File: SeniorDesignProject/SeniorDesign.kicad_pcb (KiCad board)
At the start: 2 copper layers, 69.8 x 63.5 mm, 35 parts, among them J1 RJ45(LoadCells), J2 RJ45(Accelerometer), J3 PICkit3, J5 ID-12LA Header, J6 XBEE Header, J7 7-Segment Display, P7 Power 1, U1 INA827, U2 LM1117-3.3, U3 ICL7660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

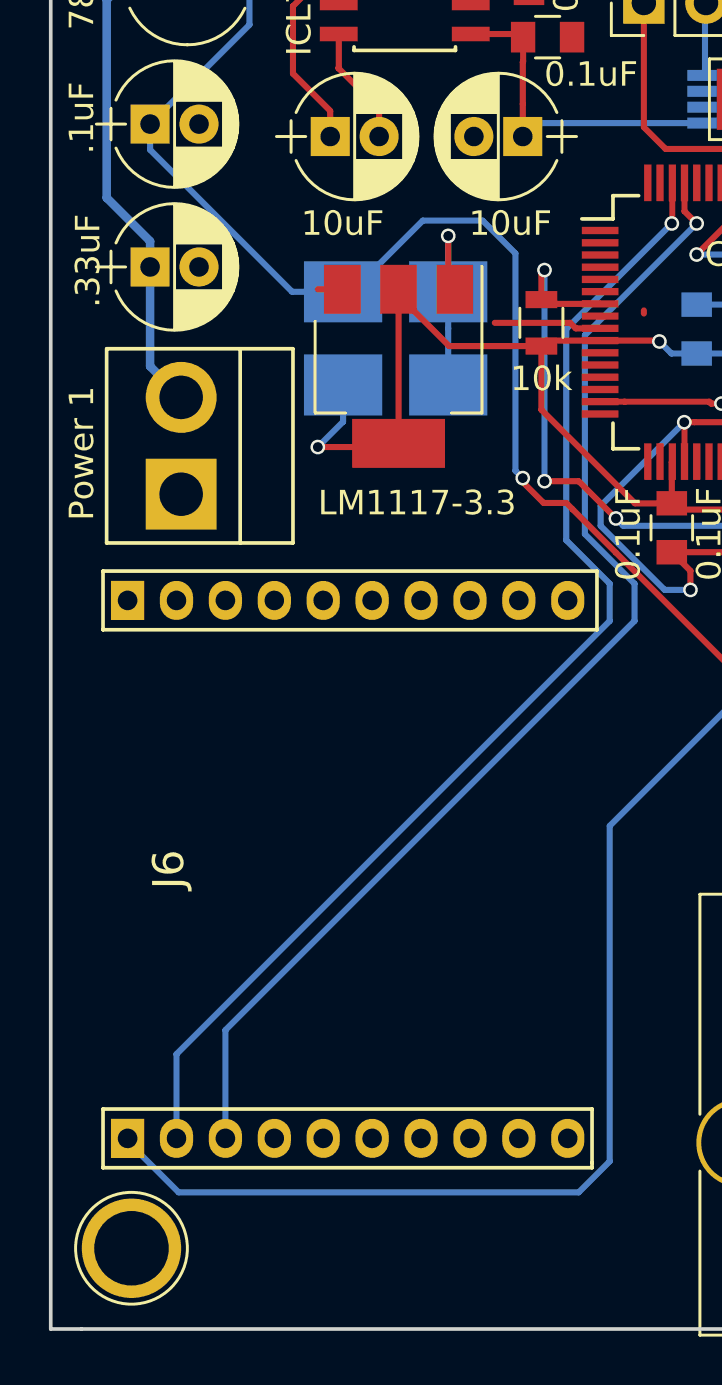
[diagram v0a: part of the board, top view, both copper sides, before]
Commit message: Version 2 updates 3.3V regulator with GND, 5V regulator with GND, and added via
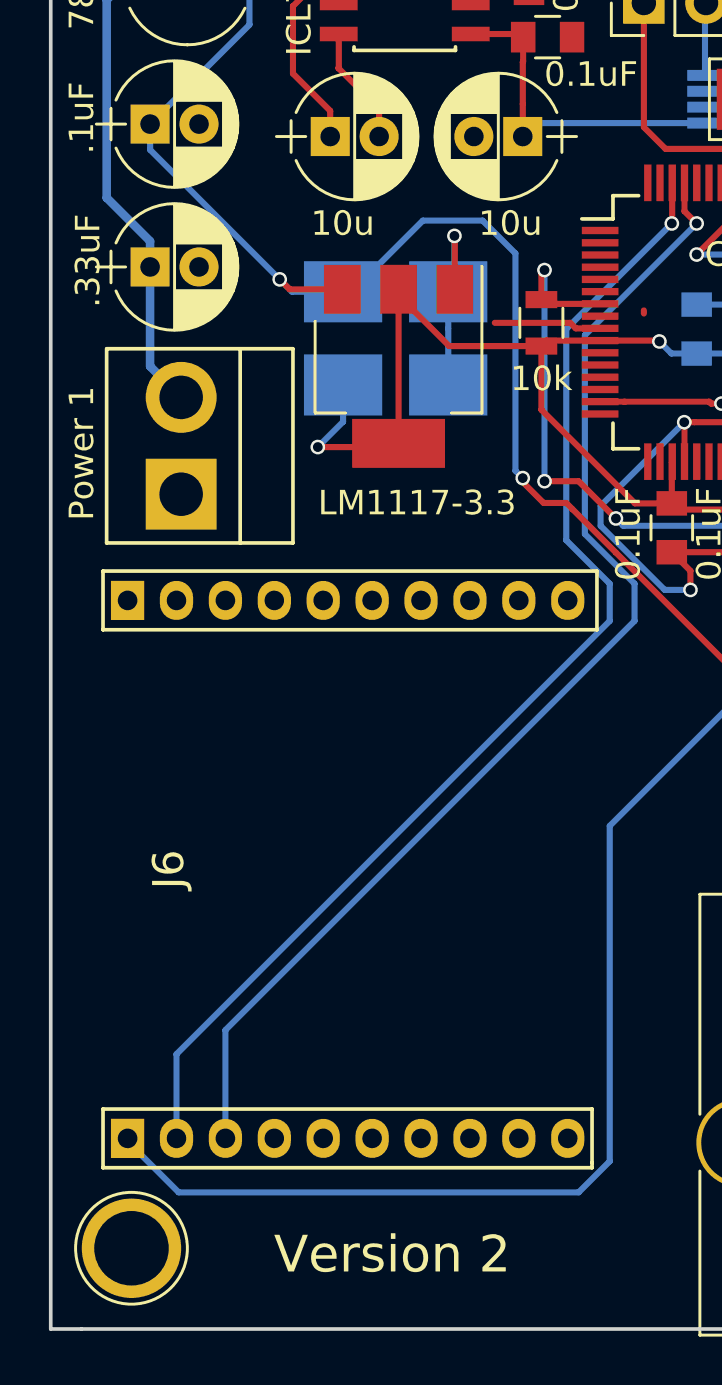
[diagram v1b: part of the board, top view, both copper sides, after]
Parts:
- C10, C9: value 10uF -> 10u
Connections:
- C13 pad 2: Net-(C13-Pad2) -> GND
- C14 pad 2: Net-(C13-Pad2) -> GND
- U2 pad 1: Net-(C13-Pad2) -> GND
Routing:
- net Net-(C13-Pad2): track 8.39 -> 3.81 mm, vias 1 -> 0
- net GND: track 35.6 -> 40.0 mm, vias 4 -> 5
- net +5V: track 143.0 -> 144.1 mm, vias 1 -> 2
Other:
- board text added: "Version 2"
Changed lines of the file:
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@@
 (kicad_pcb (version 4) (host pcbnew 4.0.6-e0-6349~53~ubuntu16.04.1)
   (general
-    (links 83)
-    (no_connects 1)
-    (area 115.494999 56.175 185.495001 121.423)
+    (links 80)
+    (no_connects 2)
+    (area 115.494999 57.074999 185.495001 120.725001)
     (thickness 1.6)
-    (drawings 7)
-    (tracks 399)
+    (drawings 8)
+    (tracks 403)
     (zones 0)
     (modules 35)
@@
     (32 B.Adhes user)
     (33 F.Adhes user)
-    (34 B.Paste user hide)
+    (34 B.Paste user)
     (35 F.Paste user)
     (36 B.SilkS user)
     (37 F.SilkS user)
-    (38 B.Mask user hide)
-    (39 F.Mask user hide)
-    (40 Dwgs.User user hide)
-    (41 Cmts.User user hide)
-    (42 Eco1.User user hide)
-    (43 Eco2.User user hide)
+    (38 B.Mask user)
+    (39 F.Mask user)
+    (40 Dwgs.User user)
+    (41 Cmts.User user)
+    (42 Eco1.User user)
+    (43 Eco2.User user)
     (44 Edge.Cuts user)
-    (45 Margin user hide)
-    (46 B.CrtYd user hide)
-    (47 F.CrtYd user hide)
+    (45 Margin user)
+    (46 B.CrtYd user)
+    (47 F.CrtYd user)
     (48 B.Fab user)
     (49 F.Fab user)
@@
     (mod_text_size 1 1)
     (mod_text_width 0.15)
-    (pad_size 1.52 1.52)
-    (pad_drill 0.8)
+    (pad_size 3.2 2.5)
+    (pad_drill 0)
     (pad_to_mask_clearance 0.2)
     (aux_axis_origin 0 0)
-    (visible_elements FFFFF7E1)
+    (visible_elements FFFFFFFF)
     (pcbplotparams
       (layerselection 0x00030_80000001)
@@
       (effects (font (size 1 1) (thickness 0.15)))
     )
-    (fp_text value 10uF (at 0.508 3.556) (layer F.SilkS)
+    (fp_text value 10u (at 0.508 3.556) (layer F.SilkS)
       (effects (font (size 1 1) (thickness 0.15)))
     )
@@
       (net 42 +5V))
     (pad 1 smd rect (at -3.15 -2.3 270) (size 2 1.5) (layers F.Cu F.Paste F.Mask)
-      (net 94 "Net-(C13-Pad2)"))
+      (net 36 GND))
     (model TO_SOT_Packages_SMD.3dshapes/SOT-223.wrl
       (at (xyz 0 0 0))
@@
       (effects (font (size 1 1) (thickness 0.15)))
     )
-    (fp_text value 10uF (at 0.508 -3.556 180) (layer F.SilkS)
+    (fp_text value 10u (at 0.508 -3.556 180) (layer F.SilkS)
       (effects (font (size 1 1) (thickness 0.15)))
     )
@@
       (net 42 +5V))
     (pad 2 smd rect (at 2.15 0) (size 3.2 2.5) (layers B.Cu B.Paste B.Mask)
-      (net 94 "Net-(C13-Pad2)"))
+      (net 36 GND))
     (model Capacitors_Tantalum_SMD.3dshapes/CP_Tantalum_Case-T_EIA-3528-12.wrl
       (at (xyz 0 0 0))
@@
       (net 38 3.3V))
     (pad 2 smd rect (at 2.15 0) (size 3.2 2.5) (layers B.Cu B.Paste B.Mask)
-      (net 94 "Net-(C13-Pad2)"))
+      (net 36 GND))
     (model Capacitors_Tantalum_SMD.3dshapes/CP_Tantalum_Case-T_EIA-3528-12.wrl
       (at (xyz 0 0 0))
@@
       (rotate (xyz 0 0 0))
     )
+  )
+  (gr_text "Version 2" (at 129.54 117.602) (layer F.SilkS)
+    (effects (font (size 1.5 1.5) (thickness 0.3)))
   )
   (gr_line (start 115.57 120.65) (end 116.84 120.65) (angle 90) (layer Edge.Cuts) (width 0.15))
@@
   )
   (segment (start 139.827 78.994) (end 139.827 79.121) (width 0.25) (layer F.Cu) (net 0))
+  (segment (start 132.08 75.946) (end 132.08 77.34159) (width 0.25) (layer B.Cu) (net 36))
+  (segment (start 132.08 77.34159) (end 131.6396 77.78199) (width 0.25) (layer B.Cu) (net 36))
+  (segment (start 131.6396 77.78199) (end 131.507795 77.913795) (width 0.25) (layer B.Cu) (net 36))
+  (segment (start 132.094 78.13) (end 132.094 75.96) (width 0.25) (layer F.Cu) (net 36))
+  (via (at 132.08 75.946) (size 0.6) (drill 0.4) (layers F.Cu B.Cu) (net 36))
+  (segment (start 132.094 75.96) (end 132.08 75.946) (width 0.25) (layer F.Cu) (net 36))
   (segment (start 141.732 90.424) (end 141.732 89.646) (width 0.25) (layer F.Cu) (net 36))
   (segment (start 141.732 89.646) (end 140.97 88.884) (width 0.25) (layer F.Cu) (net 36))
@@
   (segment (start 149.351 70.683) (end 147.701 70.683) (width 0.25) (layer B.Cu) (net 41))
   (segment (start 147.701 70.683) (end 146.726 70.683) (width 0.25) (layer B.Cu) (net 41))
+  (segment (start 125.442 78.232) (end 124.934 77.724) (width 0.25) (layer B.Cu) (net 42))
+  (segment (start 124.934 77.724) (end 119.634 72.424) (width 0.25) (layer B.Cu) (net 42))
+  (segment (start 127.494 78.13) (end 125.34 78.13) (width 0.25) (layer F.Cu) (net 42))
+  (segment (start 125.34 78.13) (end 124.934 77.724) (width 0.25) (layer F.Cu) (net 42))
+  (via (at 124.934 77.724) (size 0.6) (drill 0.4) (layers F.Cu B.Cu) (net 42))
   (segment (start 123.698 65.532) (end 123.698 67.31) (width 0.25) (layer B.Cu) (net 42))
   (segment (start 123.698 67.31) (end 119.634 71.374) (width 0.25) (layer B.Cu) (net 42))
   (segment (start 127.526 78.232) (end 125.442 78.232) (width 0.25) (layer B.Cu) (net 42))
-  (segment (start 125.442 78.232) (end 119.634 72.424) (width 0.25) (layer B.Cu) (net 42))
   (segment (start 119.634 72.424) (end 119.634 71.374) (width 0.25) (layer B.Cu) (net 42))
-  (segment (start 126.494 78.13) (end 127.494 78.13) (width 0.25) (layer F.Cu) (net 42))
   (segment (start 134.874 85.852) (end 134.574001 85.552001) (width 0.25) (layer B.Cu) (net 42))
   (segment (start 134.574001 85.552001) (end 134.574001 76.662001) (width 0.25) (layer B.Cu) (net 42))
@@
   (segment (start 130.787001 75.320999) (end 127.876 78.232) (width 0.25) (layer B.Cu) (net 42))
   (segment (start 127.876 78.232) (end 127.526 78.232) (width 0.25) (layer B.Cu) (net 42))
-  (segment (start 127.032 77.668) (end 127.494 78.13) (width 0.25) (layer F.Cu) (net 42))
   (segment (start 136.652 86.868) (end 135.726998 86.868) (width 0.25) (layer F.Cu) (net 42))
   (segment (start 135.726998 86.868) (end 134.874 86.015002) (width 0.25) (layer F.Cu) (net 42))
@@
   (segment (start 131.826 78.232) (end 131.826 79.732) (width 0.25) (layer B.Cu) (net 94))
   (segment (start 131.826 79.732) (end 131.826 82.042) (width 0.25) (layer B.Cu) (net 94))
-  (segment (start 131.826 75.946) (end 131.826 77.862) (width 0.25) (layer F.Cu) (net 94))
-  (segment (start 131.826 77.862) (end 132.094 78.13) (width 0.25) (layer F.Cu) (net 94))
-  (segment (start 131.826 78.232) (end 131.826 75.946) (width 0.25) (layer B.Cu) (net 94))
-  (via (at 131.826 75.946) (size 0.6) (drill 0.4) (layers F.Cu B.Cu) (net 94))
   (zone (net 36) (net_name GND) (layer F.Cu) (hatch edge 0.508)
     (connect_pads (clearance 0.508))

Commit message: Updates to board
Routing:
- net Net-(C13-Pad2): track 3.81 -> 0.00 mm
- net GND: track 40.0 -> 43.8 mm
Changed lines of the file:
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@@
 (kicad_pcb (version 4) (host pcbnew 4.0.6-e0-6349~53~ubuntu16.04.1)
   (general
-    (links 80)
-    (no_connects 2)
-    (area 115.494999 57.074999 185.495001 120.725001)
+    (links 84)
+    (no_connects 0)
+    (area 115.494999 56.175 185.495001 121.423)
     (thickness 1.6)
     (drawings 8)
@@
     (zones 0)
     (modules 35)
-    (nets 95)
+    (nets 94)
   )
   (page USLetter)
@@
   (net 92 "Net-(C9-Pad1)")
   (net 93 "Net-(C9-Pad2)")
-  (net 94 "Net-(C13-Pad2)")
   (net_class Default "This is the default net class."
     (clearance 0.2)
@@
     (add_net MISO)
     (add_net MOSI)
-    (add_net "Net-(C13-Pad2)")
     (add_net "Net-(C8-Pad1)")
     (add_net "Net-(C9-Pad1)")
@@
       (effects (font (size 1 1) (thickness 0.15)))
     )
-    (fp_text value 1pin (at 0 3) (layer F.Fab)
+    (fp_text value 1pin (at 0 3) (layer F.Fab) hide
       (effects (font (size 1 1) (thickness 0.15)))
     )
@@
       (effects (font (size 1 1) (thickness 0.15)))
     )
-    (fp_text value 1pin (at 0 3) (layer F.Fab)
+    (fp_text value 1pin (at 0 3) (layer F.Fab) hide
       (effects (font (size 1 1) (thickness 0.15)))
     )
@@
     (descr "module 1 pin (ou trou mecanique de percage)")
     (tags DEV)
-    (fp_text reference REF** (at 0 -3.048) (layer F.Fab)
-      (effects (font (size 1 1) (thickness 0.15)))
-    )
-    (fp_text value 1pin (at 0 3) (layer F.Fab)
+    (fp_text reference REF** (at 0 -3.048) (layer F.Fab) hide
+      (effects (font (size 1 1) (thickness 0.15)))
+    )
+    (fp_text value 1pin (at 0 3) (layer F.Fab) hide
       (effects (font (size 1 1) (thickness 0.15)))
     )
@@
     (descr "module 1 pin (ou trou mecanique de percage)")
     (tags DEV)
-    (fp_text reference REF** (at 0 -3.048) (layer F.Fab)
-      (effects (font (size 1 1) (thickness 0.15)))
-    )
-    (fp_text value 1pin (at 0 3) (layer F.Fab)
+    (fp_text reference REF** (at 0 -3.048) (layer F.Fab) hide
+      (effects (font (size 1 1) (thickness 0.15)))
+    )
+    (fp_text value 1pin (at 0 3) (layer F.Fab) hide
       (effects (font (size 1 1) (thickness 0.15)))
     )
@@
   (segment (start 144.018 78.756) (end 146.05 78.756) (width 0.25) (layer B.Cu) (net 36) (status 30))
   (segment (start 144.018 78.756) (end 141.986 78.756) (width 0.25) (layer B.Cu) (net 36) (status 30))
+  (segment (start 131.826 78.232) (end 131.826 79.732) (width 0.25) (layer B.Cu) (net 36))
+  (segment (start 131.826 79.732) (end 131.826 82.042) (width 0.25) (layer B.Cu) (net 36))
   (segment (start 142.326 71.333) (end 135.423 71.333) (width 0.25) (layer B.Cu) (net 37))
   (segment (start 135.423 71.333) (end 134.874 71.882) (width 0.25) (layer B.Cu) (net 37))
@@
   (segment (start 129 70.75063) (end 127.33737 69.088) (width 0.25) (layer F.Cu) (net 93))
   (segment (start 127.823 67.691) (end 127.348 67.691) (width 0.25) (layer F.Cu) (net 93))
-  (segment (start 131.826 78.232) (end 131.826 79.732) (width 0.25) (layer B.Cu) (net 94))
-  (segment (start 131.826 79.732) (end 131.826 82.042) (width 0.25) (layer B.Cu) (net 94))
   (zone (net 36) (net_name GND) (layer F.Cu) (hatch edge 0.508)
     (connect_pads (clearance 0.508))

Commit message: updates
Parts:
- ? (x2): value 1pin -> (none)
- ? (x2): renamed from REF**; value 1pin -> (none)
- renumbered G*** to ?
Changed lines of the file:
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@@
     (links 84)
     (no_connects 0)
-    (area 115.494999 56.175 185.495001 121.423)
+    (area 115.494999 57.074999 185.495001 120.725001)
     (thickness 1.6)
     (drawings 8)
@@
     (mod_text_size 1 1)
     (mod_text_width 0.15)
-    (pad_size 3.2 2.5)
-    (pad_drill 0)
+    (pad_size 4.064 4.064)
+    (pad_drill 3.048)
     (pad_to_mask_clearance 0.2)
     (aux_axis_origin 0 0)
@@
   (module SeniorDesignFootprints:AkronZ (layer F.Cu)
     (at 170.307 71.374)
-    (fp_text reference G*** (at -0.08 -9.45) (layer F.SilkS) hide
+    (fp_text reference "" (at -0.08 -9.45) (layer F.SilkS) hide
       (effects (font (thickness 0.3)))
     )
@@
       (effects (font (size 1 1) (thickness 0.15)))
     )
-    (fp_text value 1pin (at 0 3) (layer F.Fab) hide
+    (fp_text value "" (at 0 3) (layer F.Fab) hide
       (effects (font (size 1 1) (thickness 0.15)))
     )
@@
     (fp_circle (center 0 0) (end 2.6 0) (layer F.CrtYd) (width 0.05))
     (fp_circle (center 0 0) (end 0 -2.286) (layer F.SilkS) (width 0.12))
-    (pad 1 thru_hole circle (at 0 0) (size 4.064 4.064) (drill 3.048) (layers *.Cu *.Mask))
+    (pad "" np_thru_hole circle (at 0 0) (size 4.064 4.064) (drill 3.048) (layers *.Cu *.Mask))
   )
   (module Connectors:1pin (layer F.Cu)
@@
       (effects (font (size 1 1) (thickness 0.15)))
     )
-    (fp_text value 1pin (at 0 3) (layer F.Fab) hide
+    (fp_text value "" (at 0 3) (layer F.Fab) hide
       (effects (font (size 1 1) (thickness 0.15)))
     )
@@
     (fp_circle (center 0 0) (end 2.6 0) (layer F.CrtYd) (width 0.05))
     (fp_circle (center 0 0) (end 0 -2.286) (layer F.SilkS) (width 0.12))
-    (pad 1 thru_hole circle (at 0 0) (size 4.064 4.064) (drill 3.048) (layers *.Cu *.Mask))
+    (pad "" np_thru_hole circle (at 0 0) (size 4.064 4.064) (drill 3.048) (layers *.Cu *.Mask))
   )
   (module Connectors:1pin (layer F.Cu)
@@
     (descr "module 1 pin (ou trou mecanique de percage)")
     (tags DEV)
-    (fp_text reference REF** (at 0 -3.048) (layer F.Fab) hide
-      (effects (font (size 1 1) (thickness 0.15)))
-    )
-    (fp_text value 1pin (at 0 3) (layer F.Fab) hide
+    (fp_text reference "" (at 0 -3.048) (layer F.Fab) hide
+      (effects (font (size 1 1) (thickness 0.15)))
+    )
+    (fp_text value "" (at 0 3) (layer F.Fab) hide
       (effects (font (size 1 1) (thickness 0.15)))
     )
@@
     (fp_circle (center 0 0) (end 2.6 0) (layer F.CrtYd) (width 0.05))
     (fp_circle (center 0 0) (end 0 -2.286) (layer F.SilkS) (width 0.12))
-    (pad 1 thru_hole circle (at 0 0) (size 4.064 4.064) (drill 3.048) (layers *.Cu *.Mask))
+    (pad "" np_thru_hole circle (at 0 0) (size 4.064 4.064) (drill 3.048) (layers *.Cu *.Mask))
   )
   (module Connectors:1pin (layer F.Cu)
@@
     (descr "module 1 pin (ou trou mecanique de percage)")
     (tags DEV)
-    (fp_text reference REF** (at 0 -3.048) (layer F.Fab) hide
-      (effects (font (size 1 1) (thickness 0.15)))
-    )
-    (fp_text value 1pin (at 0 3) (layer F.Fab) hide
+    (fp_text reference "" (at 0 -3.048) (layer F.Fab) hide
+      (effects (font (size 1 1) (thickness 0.15)))
+    )
+    (fp_text value "" (at 0 3) (layer F.Fab) hide
       (effects (font (size 1 1) (thickness 0.15)))
     )
@@
     (fp_circle (center 0 0) (end 2.6 0) (layer F.CrtYd) (width 0.05))
     (fp_circle (center 0 0) (end 0 -2.286) (layer F.SilkS) (width 0.12))
-    (pad 1 thru_hole circle (at 0 0) (size 4.064 4.064) (drill 3.048) (layers *.Cu *.Mask))
+    (pad "" np_thru_hole circle (at 0 0) (size 4.064 4.064) (drill 3.048) (layers *.Cu *.Mask))
   )
   (module Housings_SOIC:SOIC-8_3.9x4.9mm_Pitch1.27mm (layer F.Cu)
